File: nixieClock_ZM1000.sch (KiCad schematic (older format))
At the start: 3 parts

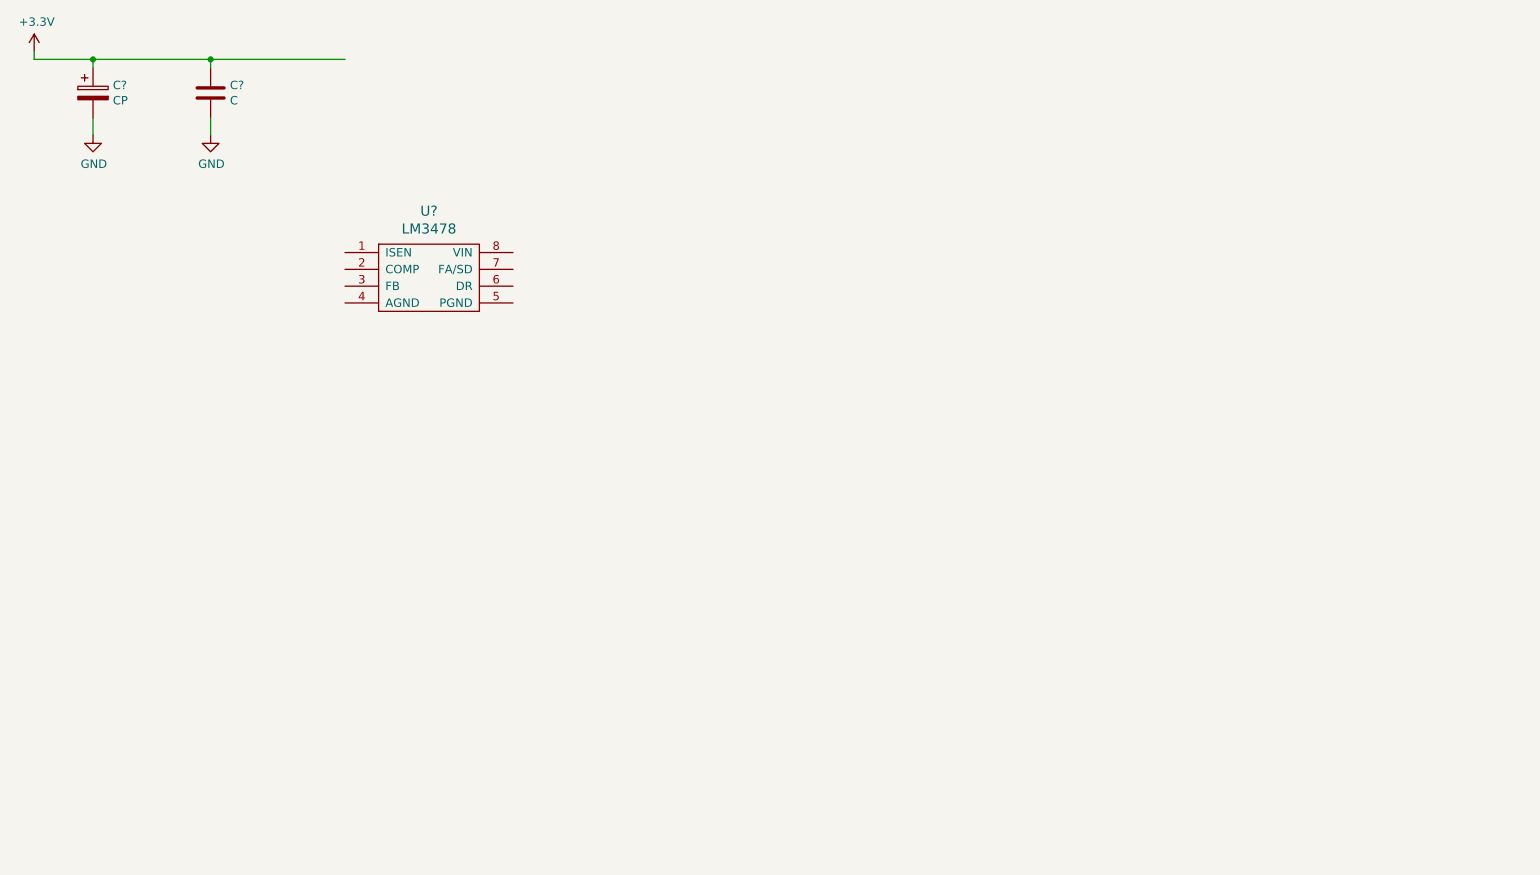
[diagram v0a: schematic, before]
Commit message: Inserted PSU
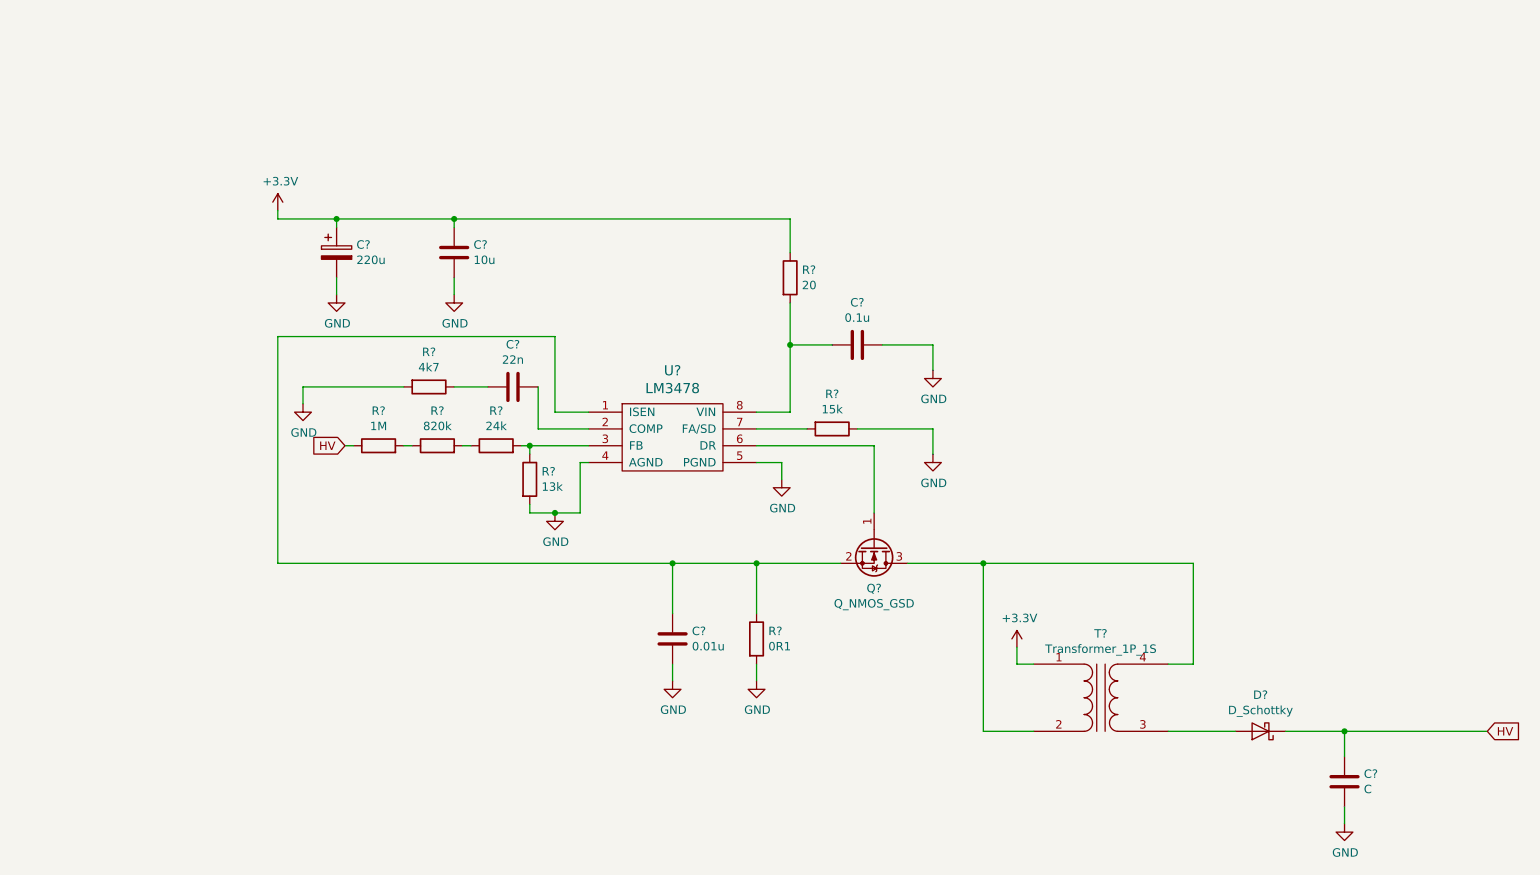
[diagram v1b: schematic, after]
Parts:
- added C?: 22n, symbol Device:C
- added C?: 0.01u, symbol Device:C
- added C?: 0.1u, symbol Device:C
- added C?: C, symbol Device:C
- added D?: D_Schottky, symbol Device:D_Schottky
- added Q?: Q_NMOS_GSD, symbol Device:Q_NMOS_GSD
- added R?: 4k7, symbol Device:R
- added R?: 0R1, symbol Device:R
- added R?: 15k, symbol Device:R
- added R?: 20, symbol Device:R
- added R?: 1M, symbol Device:R
- added R?: 820k, symbol Device:R
- added R?: 24k, symbol Device:R
- added R?: 13k, symbol Device:R
- added T?: Transformer_1P_1S, symbol Device:Transformer_1P_1S
- C?: value CP -> 220u
- C?: value C -> 10u
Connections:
- net labels added: HV
- wire segments 8 -> 62
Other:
- moved on the sheet: C?, U?
